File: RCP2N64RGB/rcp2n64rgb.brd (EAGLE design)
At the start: 149.4 x 21.1 mm, 65 parts, among them U1 74VHC9151FT, U2 SN74LVC1G17DCKR

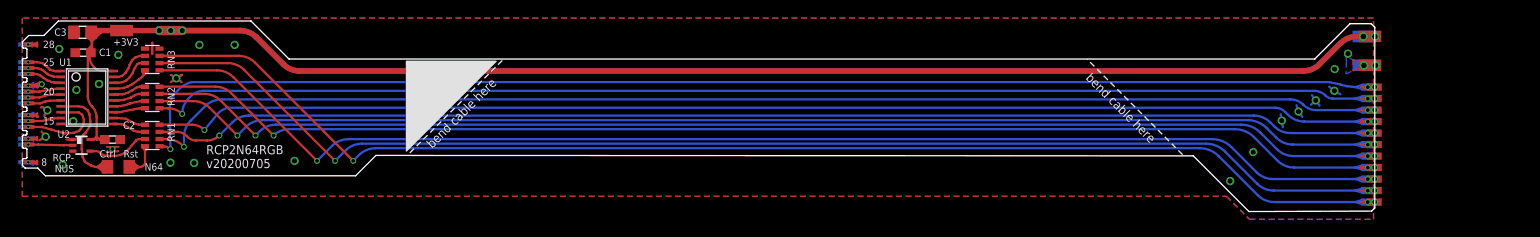
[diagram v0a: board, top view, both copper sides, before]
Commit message: increase flex by 1.5cm for easier routing
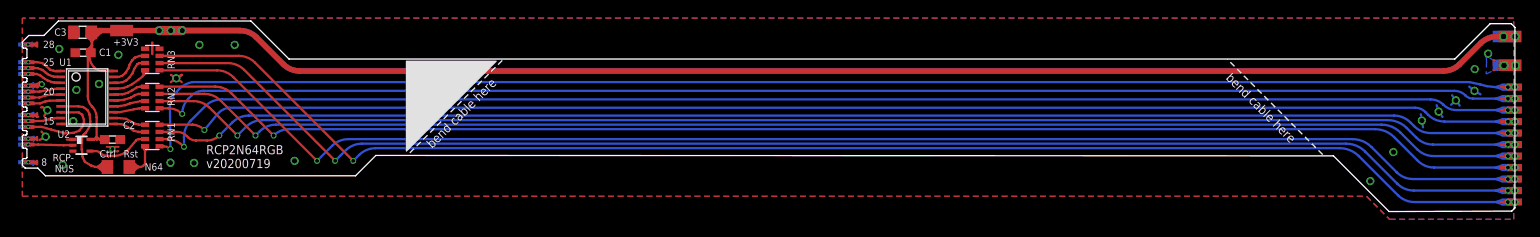
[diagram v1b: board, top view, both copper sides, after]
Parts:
- moved /RST_A 15.5 mm to (164.2, 6.35)
- moved CLOCK# 15.5 mm to (164.2, 3.81)
- moved CTRL_A 15.5 mm to (164.2, 5.08)
- moved D0 15.5 mm to (164.2, -6.35)
- moved D1 15.5 mm to (164.2, -5.08)
- moved D2 15.5 mm to (164.2, -3.81)
- moved D3 15.5 mm to (164.2, -2.54)
- moved D4 15.5 mm to (164.2, -1.27)
- moved D5 15.5 mm to (164.2, 0.00)
- moved D6 15.5 mm to (164.2, 1.27)
- moved DSYNC# 15.5 mm to (164.2, 2.54)
- moved P_GND1 15.5 mm to (164.3, 8.76)
- moved P_VCC_3V1 15.5 mm to (164.3, 11.9)
- moved /RST_A1 15.5 mm to (164.8, 6.35)
- moved CLOCK#1 15.5 mm to (164.8, 3.81)
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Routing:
- net 3V3: track 305.7 -> 336.6 mm
- net D3.1: track 145.4 -> 160.9 mm
- net D0.1: track 149.0 -> 164.5 mm
- net D1.1: track 148.2 -> 163.7 mm
- net VCLK.1: track 144.6 -> 160.1 mm
- net D6.1: track 144.2 -> 159.7 mm
- net D5.1: track 144.5 -> 160.0 mm
- net D4.1: track 145.0 -> 160.5 mm
- net CTRL.1: track 143.7 -> 159.1 mm
- net #DSYNC.1: track 144.0 -> 159.4 mm
- net RST.1: track 149.0 -> 164.4 mm
- net D2.1: track 148.1 -> 163.5 mm
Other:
- board size 149.4 x 21.1 mm -> 164.9 x 21.1 mm
- board text added: "RCP2N64RGB v20200719"
- board text removed: "RCP2N64RGB v20200705"
